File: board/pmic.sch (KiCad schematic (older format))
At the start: 80 parts, among them J10 USB_MICRO_B, J11 DB9, J12 RJ45, P48 CONN_6, P49 CONN_2, U17 MAX4377, U18 MAX4378, U19 PIC18F85J50, U20 MAX3227, U21 MAX3490, X2 CRYSTAL

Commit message: Issue #1022 - Schematics final changes.
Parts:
- removed R140: R, ~, symbol R
- removed R307: 1.5K, ~, symbol R
- removed U19: PIC18F85J50, ~, symbol PIC18F85J50
- added D34, D35, D36, D37, D38, D39: LED, ~, symbol LED
- added R307: 1K, ~, symbol RES_NET4
- added R339, R340, R341: 2.2K, ~, symbol R
- added U19: PIC18F85J94, ~, symbol PIC18F85J94
- R119: value 6.8K -> 47K
- R120: value 2.2K -> 4.7K
- R123: value 1.5K -> 21K
- R124: value 2.2K -> 5.7K
- R133: value 2.2K -> 10K
- R134, R136: value R -> 4.7K
- R135: value 2.2K -> 3.3K
- R137: value 2.2K -> 1K
- R138: value R -> 10K
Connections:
- net labels added: IR SENSE, IR-LED, L-FPGA-1, L-FPGA-2, L-GRX-A, L-GRX-D, L-GRX-E, L-GRX-M, L-GTX-A, L-GTX-D, L-GTX-E, L-GTX-M, L-PGOOD, L-RX1-A, L-RX1-C, L-RX1-D, L-RX1-E, L-RX2-A, L-RX2-C, L-RX2-D, L-RX2-E, L-TX1-A, L-TX1-C, L-TX1-D, L-TX1-E, L-TX2-A, L-TX2-C, L-TX2-D, L-TX2-E, L-USB-E, L-V-A, L-V-D, L-V-E
- net labels removed: INVALID, LED1, LED10, LED11, LED12, LED13, LED14, LED15, LED16, LED17, LED18, LED19, LED2, LED20, LED21, LED22, LED23, LED24, LED25, LED3, LED4, LED5, LED6, LED7, LED8, LED9, READY
- wire segments 244 -> 254
- no-connect marks 17 -> 11
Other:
- note added: "ICSP HEADER"
- note added: "PIC FWUP"
- note added: "RESET STATUS LED"
- note added: "USB HEADER"
- note removed: "NOT POPULATED"
- moved on the sheet: C183, D27

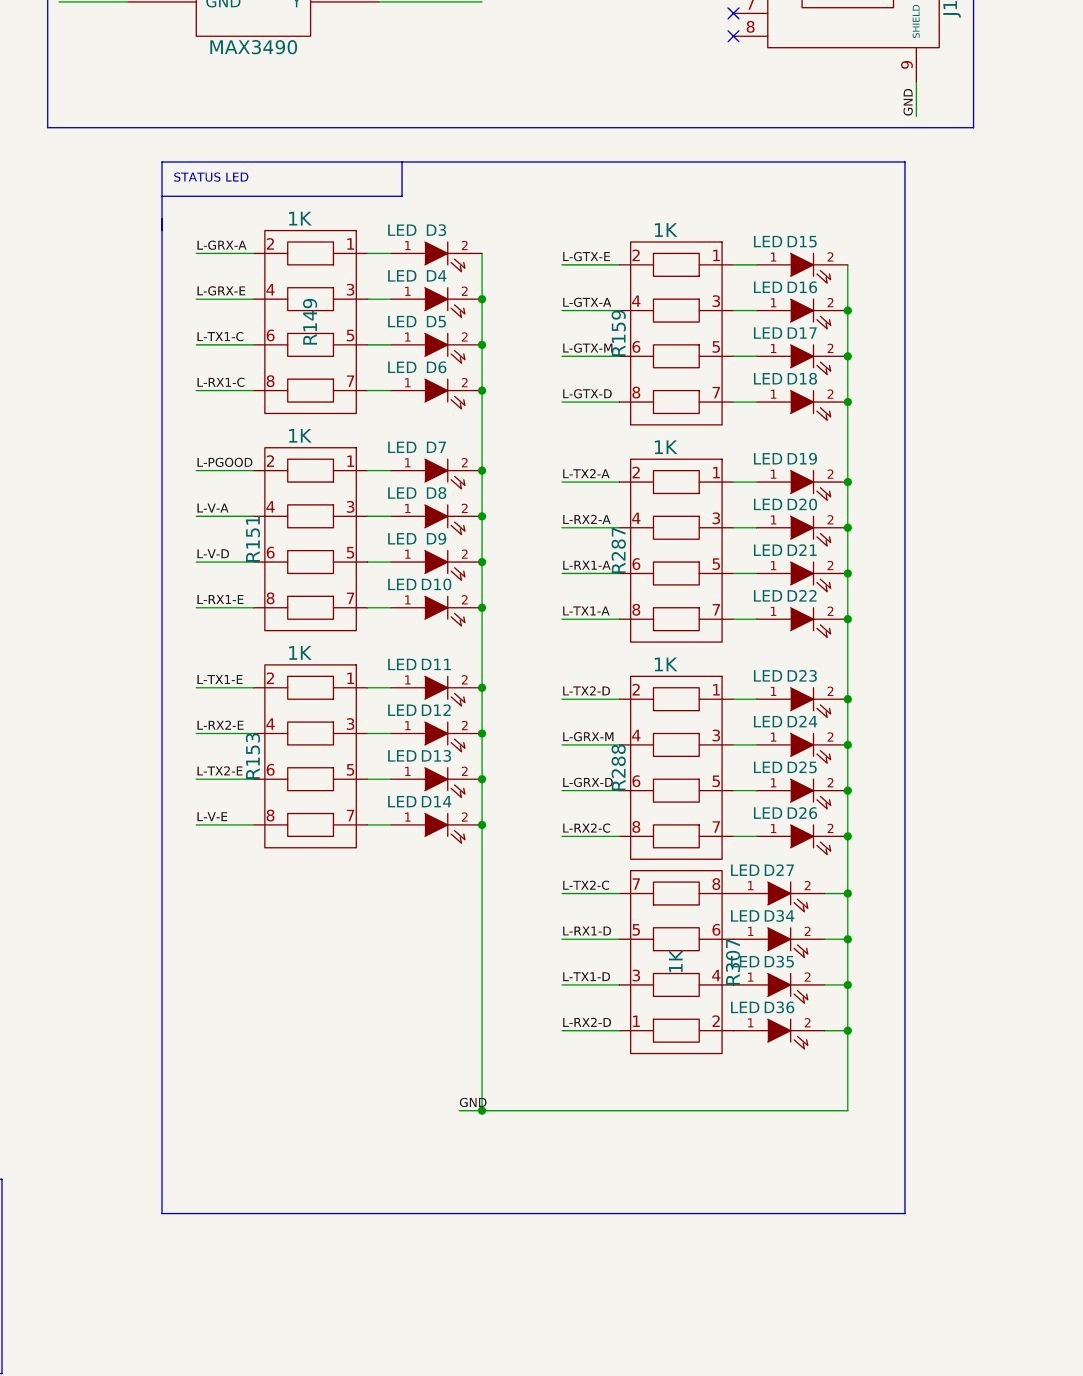
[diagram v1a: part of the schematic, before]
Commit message: Issue #1027 - Schematics final changes.
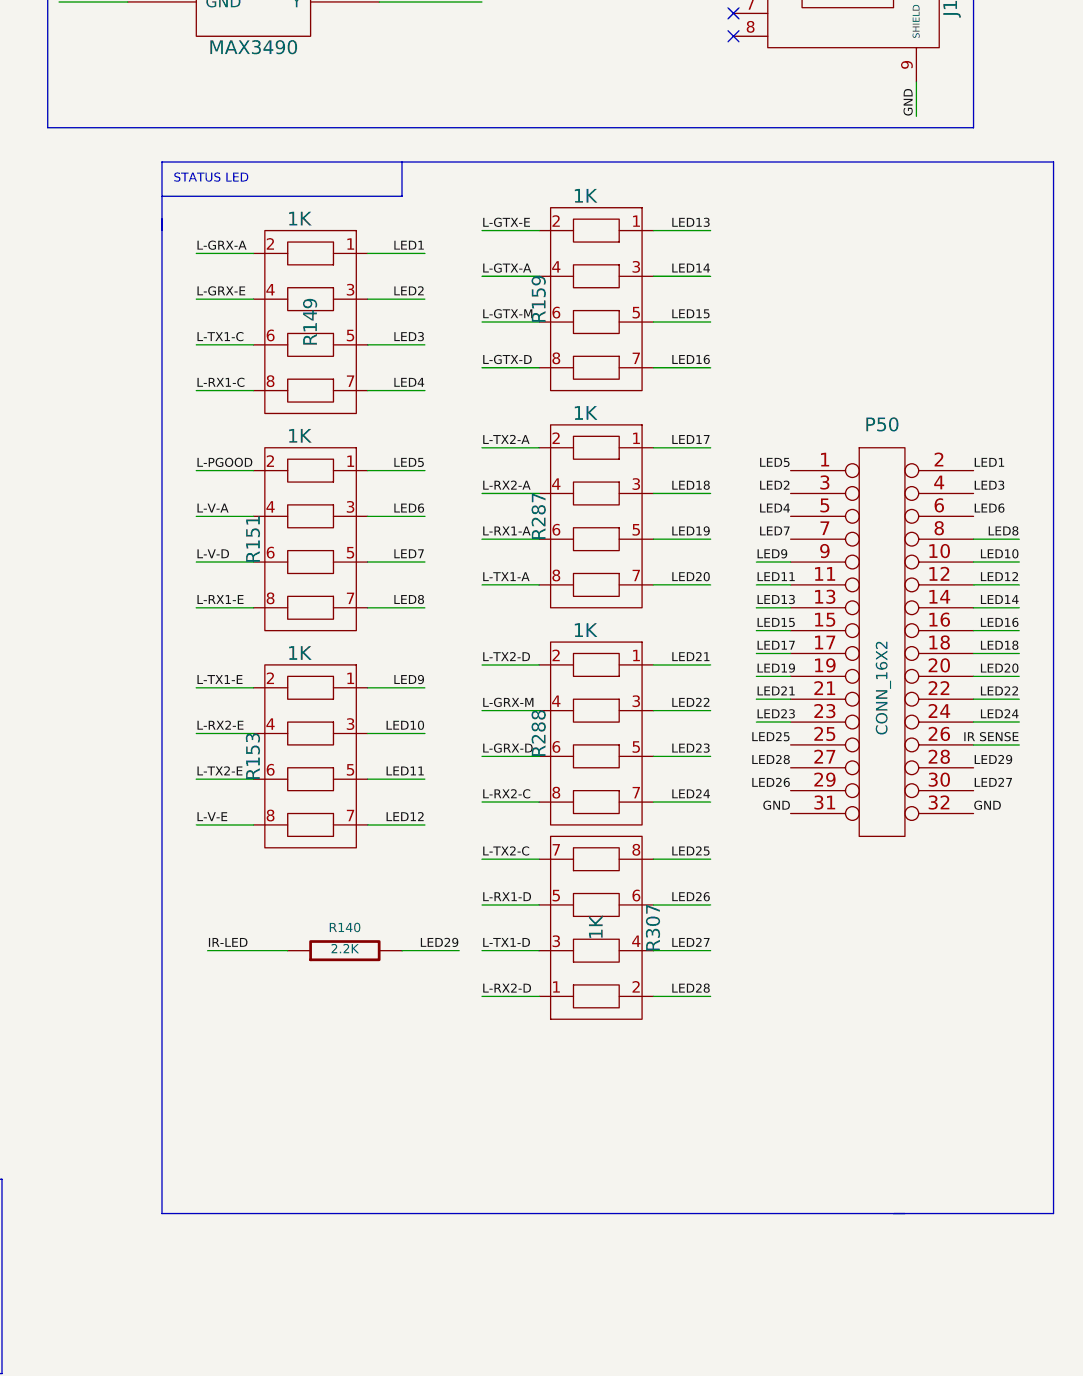
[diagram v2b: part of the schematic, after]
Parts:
- removed D10, D11, D12, D13, D14, D15, D16, D17, D18, D19, D20, D21, D22, D23, D24, D25, D26, D27, D3, D34, D35, D36, D4, D5, D6, D7, D8, D9: LED, ~, symbol LED
- added P50: CONN_16X2, symbol CONN_16X2
- added R140: 2.2K, ~, symbol R
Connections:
- net labels added: LED1, LED10, LED11, LED12, LED13, LED14, LED15, LED16, LED17, LED18, LED19, LED2, LED20, LED21, LED22, LED23, LED24, LED25, LED26, LED27, LED28, LED29, LED3, LED4, LED5, LED6, LED7, LED8, LED9
- wire segments 254 -> 271
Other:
- moved on the sheet: R159, R287, R288, R307

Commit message: Issue #1027 - Schematics final changes.
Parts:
- removed C204: 0.1mfd, ~, symbol C
- removed J10: USB_MICRO_B, ~, symbol USB_MICRO_B
- removed P49: CONN_2, symbol CONN_2
- removed R147: 10K, ~, symbol R
- removed VR1, VR2: VR, ~, symbol VR
- added GS1: GS2, symbol GS2
- added P51: CONN_4, symbol CONN_4
- added R360: 10K, ~, symbol R
- added R361, R362, R363, R364, R365, R366: 4.7K, ~, symbol R
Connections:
- net labels added: 232-FON, 232-INV, 232-RDY, LED-GRX-A, LED-GRX-D, LED-GRX-E, LED-GRX-M, LED-GTX-A, LED-GTX-D, LED-GTX-E, LED-GTX-M, LED-IR, LED-PGOOD, LED-RX1-A, LED-RX1-C, LED-RX1-D, LED-RX1-E, LED-RX2-A, LED-RX2-C, LED-RX2-D, LED-RX2-E, LED-TX1-A, LED-TX1-C, LED-TX1-D, LED-TX1-E, LED-TX2-A, LED-TX2-C, LED-TX2-D, LED-TX2-E, LED-V-A, LED-V-D, LED-V-E, PIC-OSC1
- net labels removed: L-FPGA-1, L-FPGA-2, L-USB-E, LED1, LED10, LED11, LED12, LED13, LED14, LED15, LED16, LED17, LED18, LED19, LED2, LED20, LED21, LED22, LED23, LED24, LED25, LED26, LED27, LED28, LED29, LED3, LED4, LED5, LED6, LED7, LED8, LED9
- wire segments 271 -> 251
- no-connect marks 11 -> 9
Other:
- note removed: "PIC FWUP"
- moved on the sheet: C173, C174, D37, D38, D39, P50, R140, R149, R151, R153, R159, R287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

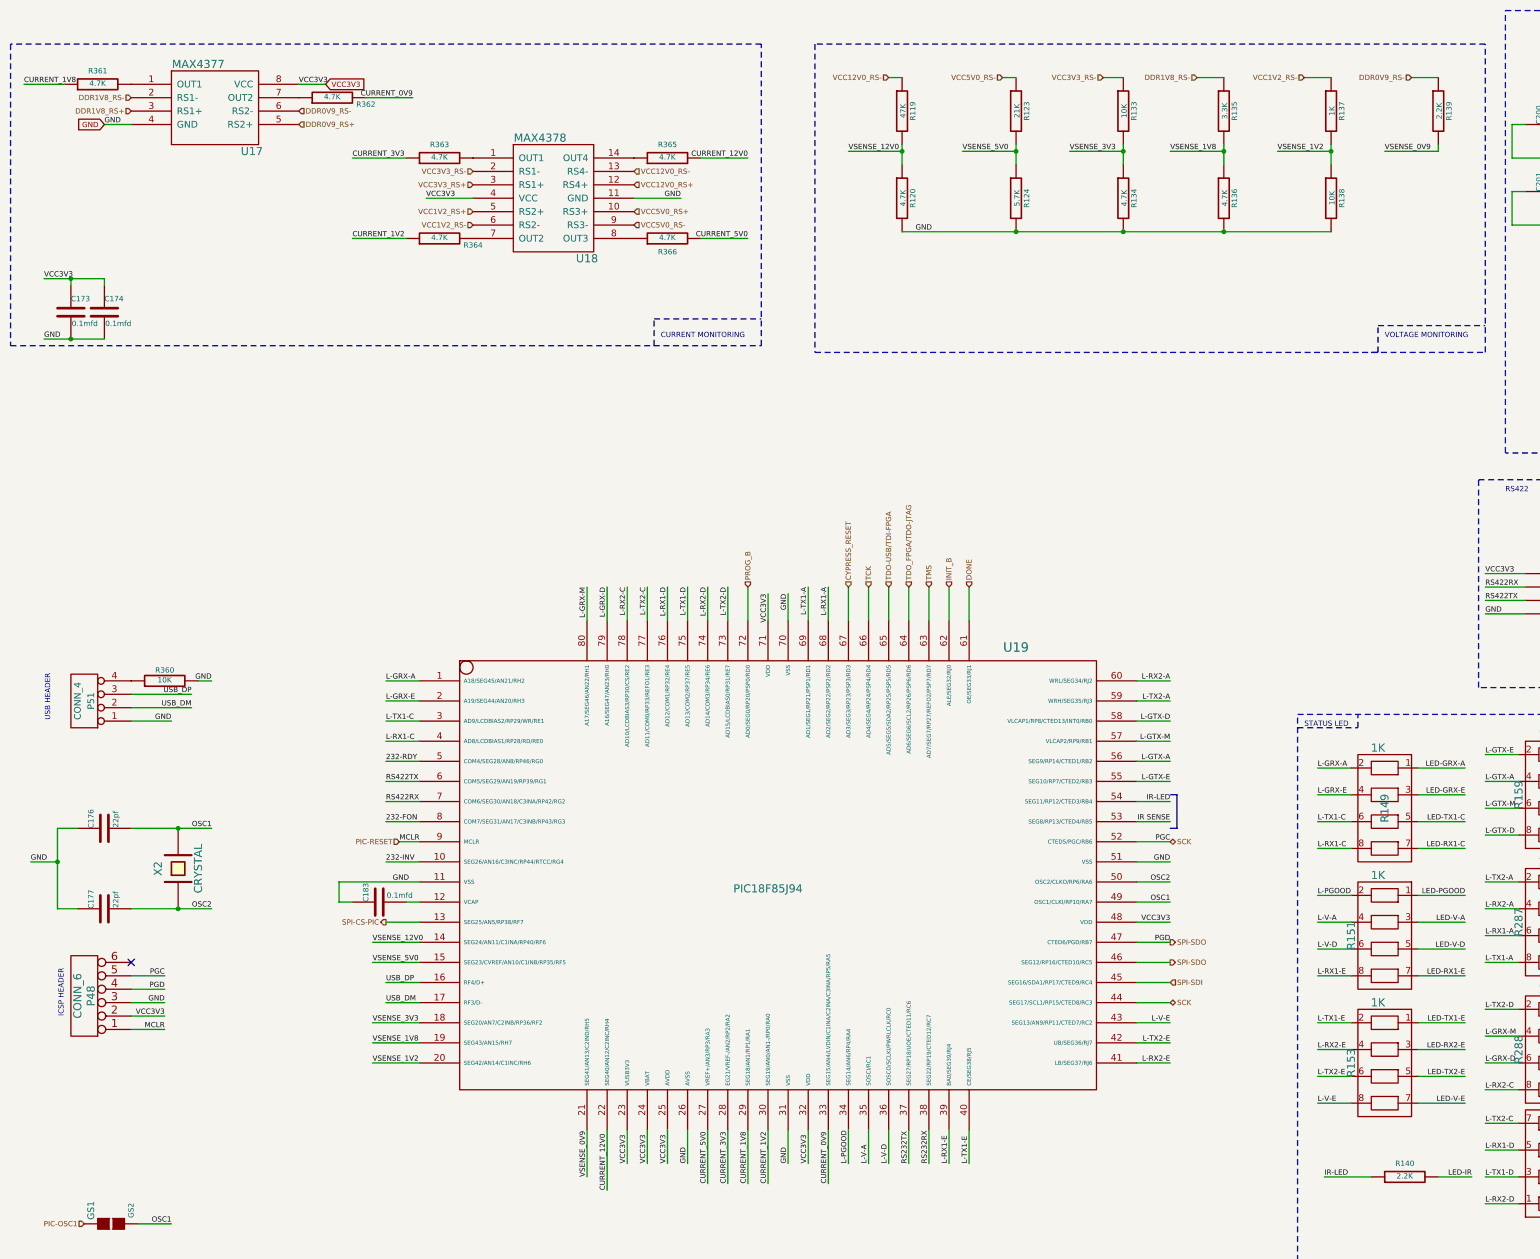
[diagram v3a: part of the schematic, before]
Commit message: Issue #1027 - Schematics final changes.
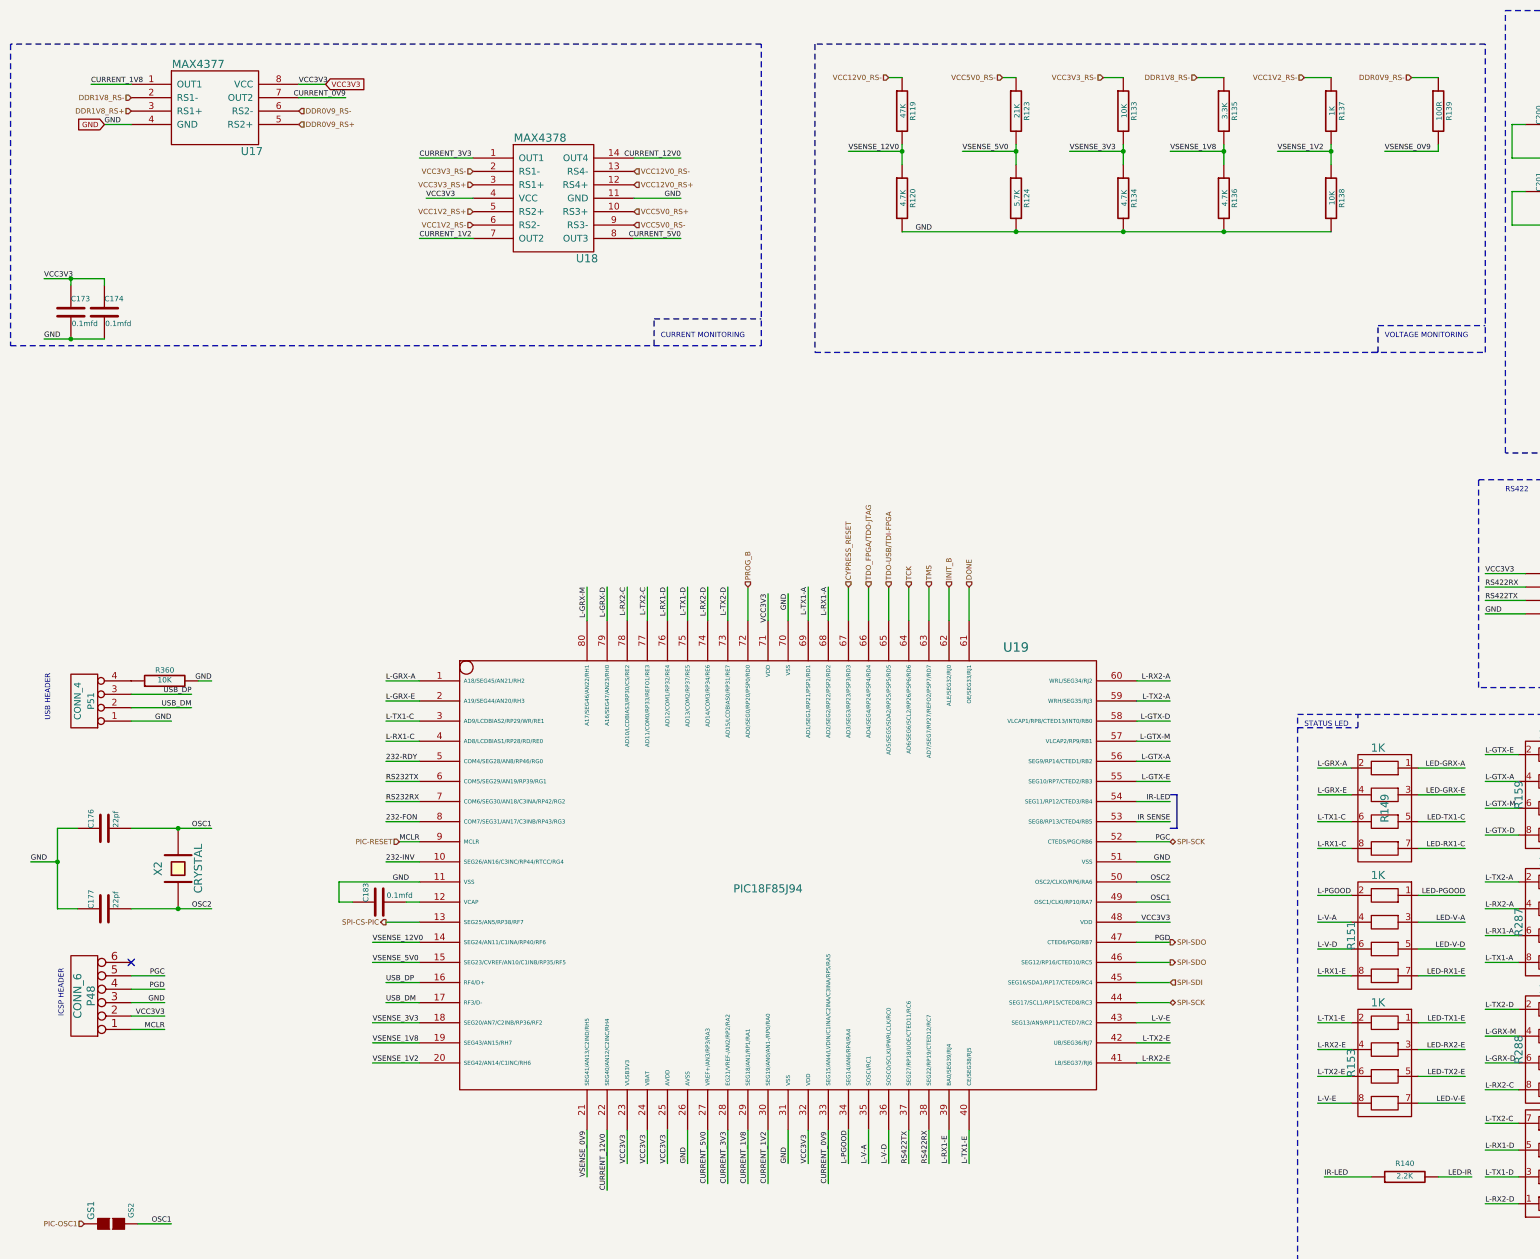
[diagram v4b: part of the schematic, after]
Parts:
- removed R361, R362, R363, R364, R365, R366: 4.7K, ~, symbol R
- R139: value 2.2K -> 100R
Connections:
- net CURRENT_0V9: now also U17.7 (OUT2)
- net CURRENT_12V0: now also U18.14 (OUT4)
- net CURRENT_1V2: now also U18.7 (OUT2)
- net CURRENT_1V8: now also U17.1 (OUT1)
- net CURRENT_3V3: now also U18.1 (OUT1)
- net CURRENT_5V0: now also U18.8 (OUT3)
- net RS232RX: now also U19.7 (COM6/SEG30/AN18/C3INA/RP42/RG2); no longer U19.38 (SEG22/RP19/CTED12/RC7)
- net RS232TX: now also U19.6 (COM5/SEG29/AN19/RP39/RG1); no longer U19.37 (SEG27/RP18/UOE/CTED11/RC6)
- net RS422RX: now also U19.38 (SEG22/RP19/CTED12/RC7); no longer U19.7 (COM6/SEG30/AN18/C3INA/RP42/RG2)
- net RS422TX: now also U19.37 (SEG27/RP18/UOE/CTED11/RC6); no longer U19.6 (COM5/SEG29/AN19/RP39/RG1)
- net TCK: now also U19.64 (AD6/SEG6/SCL2/RP26/PSP6/RD6); no longer U19.66 (AD4/SEG4/RP24/PSP4/RD4)
- net TDO_FPGA/TDO-JTAG: now also U19.66 (AD4/SEG4/RP24/PSP4/RD4); no longer U19.64 (AD6/SEG6/SCL2/RP26/PSP6/RD6)
- net SCK renamed SPI-SCK
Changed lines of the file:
@@
 Sheet 7 8
 Title "HDMI2USB"
-Date "11 apr 2014"
+Date "15 apr 2014"
 Rev ""
 Comp ""
@@
 Text Label 1300 1350 0    39   ~ 0
 GND
-Text Label 6100 1600 2    39   ~ 0
+Text Label 5600 1600 2    39   ~ 0
 CURRENT_12V0
-Text Label 6100 2200 2    39   ~ 0
+Text Label 5600 2200 2    39   ~ 0
 CURRENT_5V0
-Text Label 3150 1600 0    39   ~ 0
+Text Label 3650 1600 0    39   ~ 0
 CURRENT_3V3
-Text Label 3150 2200 0    39   ~ 0
+Text Label 3650 2200 0    39   ~ 0
 CURRENT_1V2
-Text Label 3600 1150 2    39   ~ 0
+Text Label 3100 1150 2    39   ~ 0
 CURRENT_0V9
-Text Label 700  1050 0    39   ~ 0
+Text Label 1200 1050 0    39   ~ 0
 CURRENT_1V8
 Text HLabel 5250 1800 2    39   Input ~ 0
@@
 Text Label 9250 7000 2    39   ~ 0
 OSC2
+Text Label 3400 6250 0    39   ~ 0
+RS232TX
+Text Label 3400 6400 0    39   ~ 0
+RS232RX
 Text Label 7300 9100 1    39   ~ 0
-RS232TX
+RS422TX
 Text Label 7450 9100 1    39   ~ 0
-RS232RX
-Text Label 3400 6250 0    39   ~ 0
-RS422TX
-Text Label 3400 6400 0    39   ~ 0
 RS422RX
 Text HLabel 9250 7600 2    39   Output ~ 0
@@
 SPI-SDI
 Text HLabel 9250 7900 2    39   BiDi ~ 0
-SCK
+SPI-SCK
 Text HLabel 3400 7300 0    39   Output ~ 0
 SPI-CS-PIC
@@
 Text HLabel 7450 4800 1    39   Input ~ 0
 TMS
-Text HLabel 7000 4800 1    39   Input ~ 0
+Text HLabel 7300 4800 1    39   Input ~ 0
 TCK
 Text HLabel 7150 4800 1    39   Input ~ 0
 TDO-USB/TDI-FPGA
-Text HLabel 7300 4800 1    39   Input ~ 0
+Text HLabel 7000 4800 1    39   Input ~ 0
 TDO_FPGA/TDO-JTAG
 Text HLabel 6100 4800 1    39   Input ~ 0
@@
 P 11250 1250
 F 0 "R139" V 11330 1250 40  0000 C CNN
-F 1 "2.2K" V 11257 1251 40  0000 C CNN
+F 1 "100R" V 11257 1251 40  0000 C CNN
 F 2 "~" V 11180 1250 30  0000 C CNN
 F 3 "~" H 11250 1250 30  0000 C CNN
@@
 SPI-SDO
 Text HLabel 9250 6700 2    39   BiDi ~ 0
-SCK
+SPI-SCK
 Text Notes 1000 7650 3    39   ~ 0
 ICSP HEADER
@@
 Text Label 12150 3000 0    39   ~ 0
 232-RDY
-$Comp
-L R R361
-U 1 1 534D6677
-P 1250 1050
-F 0 "R361" V 1350 1050 40  0000 C CNN
-F 1 "4.7K" V 1257 1051 40  0000 C CNN
-F 2 "~" V 1180 1050 30  0000 C CNN
-F 3 "~" H 1250 1050 30  0000 C CNN
-	1    1250 1050
-	0    -1   -1   0
-$EndComp
-$Comp
-L R R362
-U 1 1 534D6690
-P 3000 1150
-F 0 "R362" V 2950 900 40  0000 C CNN
-F 1 "4.7K" V 3007 1151 40  0000 C CNN
-F 2 "~" V 2930 1150 30  0000 C CNN
-F 3 "~" H 3000 1150 30  0000 C CNN
-	1    3000 1150
-	0    -1   -1   0
-$EndComp
-$Comp
-L R R364
-U 1 1 534D6697
-P 3800 2200
-F 0 "R364" V 3750 1950 40  0000 C CNN
-F 1 "4.7K" V 3807 2201 40  0000 C CNN
-F 2 "~" V 3730 2200 30  0000 C CNN
-F 3 "~" H 3800 2200 30  0000 C CNN
-	1    3800 2200
-	0    -1   -1   0
-$EndComp
-$Comp
-L R R363
-U 1 1 534D669D
-P 3800 1600
-F 0 "R363" V 3900 1600 40  0000 C CNN
-F 1 "4.7K" V 3807 1601 40  0000 C CNN
-F 2 "~" V 3730 1600 30  0000 C CNN
-F 3 "~" H 3800 1600 30  0000 C CNN
-	1    3800 1600
-	0    -1   -1   0
-$EndComp
-$Comp
-L R R365
-U 1 1 534D66A3
-P 5500 1600
-F 0 "R365" V 5600 1600 40  0000 C CNN
-F 1 "4.7K" V 5507 1601 40  0000 C CNN
-F 2 "~" V 5430 1600 30  0000 C CNN
-F 3 "~" H 5500 1600 30  0000 C CNN
-	1    5500 1600
-	0    -1   -1   0
-$EndComp
-Wire Wire Line
-	3600 1150 3250 1150
-Wire Wire Line
-	1000 1050 700  1050
-Wire Wire Line
-	3150 1600 3550 1600
-Wire Wire Line
-	3150 2200 3550 2200
-$Comp
-L R R366
-U 1 1 534D6C07
-P 5500 2200
-F 0 "R366" V 5400 2200 40  0000 C CNN
-F 1 "4.7K" V 5507 2201 40  0000 C CNN
-F 2 "~" V 5430 2200 30  0000 C CNN
-F 3 "~" H 5500 2200 30  0000 C CNN
-	1    5500 2200
-	0    -1   -1   0
-$EndComp
-Wire Wire Line
-	5750 1600 6100 1600
-Wire Wire Line
-	5750 2200 6100 2200
+Wire Wire Line
+	3100 1150 2750 1150
+Wire Wire Line
+	1500 1050 1200 1050
+Wire Wire Line
+	3650 1600 4050 1600
+Wire Wire Line
+	3650 2200 4050 2200
+Wire Wire Line
+	5250 1600 5600 1600
+Wire Wire Line
+	5250 2200 5600 2200
 Wire Wire Line
 	4050 1900 3700 1900
